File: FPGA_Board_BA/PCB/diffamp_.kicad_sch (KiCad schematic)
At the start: 15 parts, among them U20 1819_IS8

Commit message: schematic fixes after Leo Meeting
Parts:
- removed R108, R110: 9k1_0603, Resistor_SMD:R_0603_1608Metric, symbol WLIB_R:9k1_0603
- removed R109: 1k_0603, Resistor_SMD:R_0603_1608Metric, symbol WLIB_R:1k_0603
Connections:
- net Analog: now also R106.2, U20.3 (+)
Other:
- note removed: "R1"
- note removed: "R2"

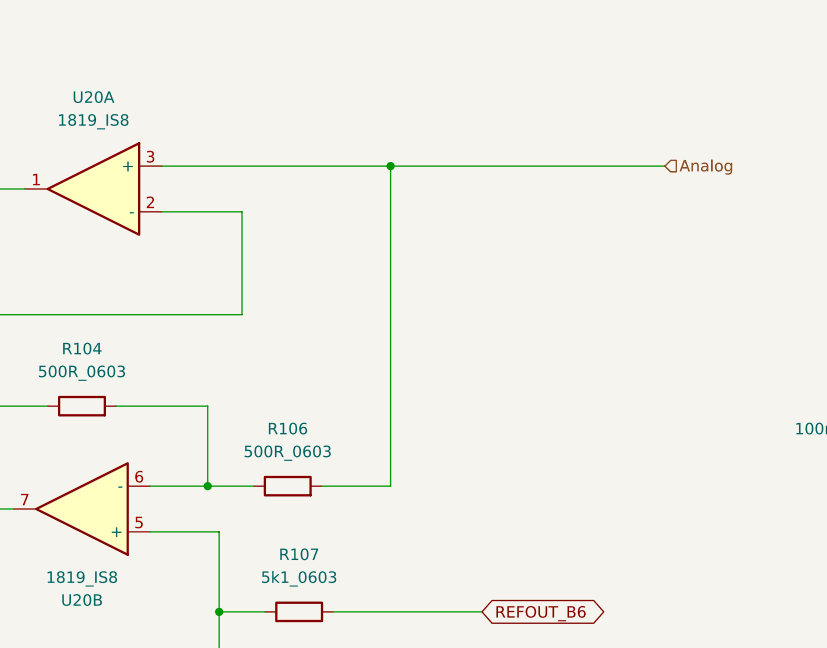
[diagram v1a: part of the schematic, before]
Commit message: placement of Power DCDC and Buffers ready
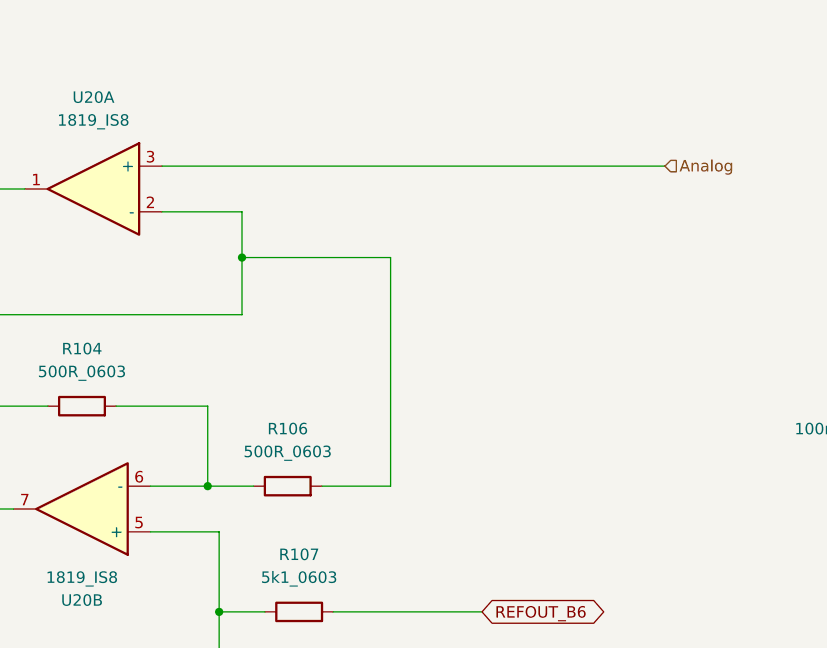
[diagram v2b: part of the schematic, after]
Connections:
- net Analog: no longer R106.2
- net at R102.2, U20.1, U20.2 (-): now also R106.2
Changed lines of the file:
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@@
-	)
-	(junction
-		(at 158.75 78.74)
-		(diameter 0)
-		(color 0 0 0 0)
 	)
 	(junction
@@
 	)
 	(junction
+		(at 142.24 88.9)
+		(diameter 0)
+		(color 0 0 0 0)
+	)
+	(junction
 		(at 81.28 134.62)
 		(diameter 0)
@@
 	(wire
 		(pts
-			(xy 142.24 83.82) (xy 142.24 95.25)
+			(xy 142.24 83.82) (xy 142.24 88.9)
 		)
 		(stroke
@@
 	(wire
 		(pts
-			(xy 158.75 78.74) (xy 158.75 114.3)
-		)
-		(stroke
-			(width 0)
-			(type default)
-		)
-	)
-	(wire
-		(pts
 			(xy 158.75 114.3) (xy 151.13 114.3)
 		)
@@
 	(wire
 		(pts
-			(xy 158.75 78.74) (xy 189.23 78.74)
+			(xy 133.35 78.74) (xy 189.23 78.74)
 		)
 		(stroke
@@
 	(wire
 		(pts
+			(xy 158.75 114.3) (xy 158.75 88.9)
+		)
+		(stroke
+			(width 0)
+			(type default)
+		)
+	)
+	(wire
+		(pts
 			(xy 222.25 120.65) (xy 222.25 124.46)
 		)
@@
 	(wire
 		(pts
+			(xy 142.24 88.9) (xy 142.24 95.25)
+		)
+		(stroke
+			(width 0)
+			(type default)
+		)
+	)
+	(wire
+		(pts
 			(xy 86.36 116.84) (xy 86.36 123.19)
 		)
@@
 	(wire
 		(pts
-			(xy 133.35 78.74) (xy 158.75 78.74)
-		)
-		(stroke
-			(width 0)
-			(type default)
-		)
-	)
-	(wire
-		(pts
 			(xy 222.25 120.65) (xy 227.33 120.65)
 		)
@@
 		)
 		(stroke
+			(width 0)
+			(type default)
+		)
+	)
+	(wire
+		(pts
+			(xy 158.75 88.9) (xy 142.24 88.9)
+		)
+		(stroke
